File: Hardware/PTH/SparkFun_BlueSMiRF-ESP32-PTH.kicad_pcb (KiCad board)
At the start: 2 copper layers, 38.1 x 15.2 mm, 45 parts, among them J2 Conn_01x06, Q1 Q_NMOS_DGS, Q2 Q_NMOS_DGS, SW1 Switch, U1 ESP32_Pico_Mini, U2 AP2112K-3.3

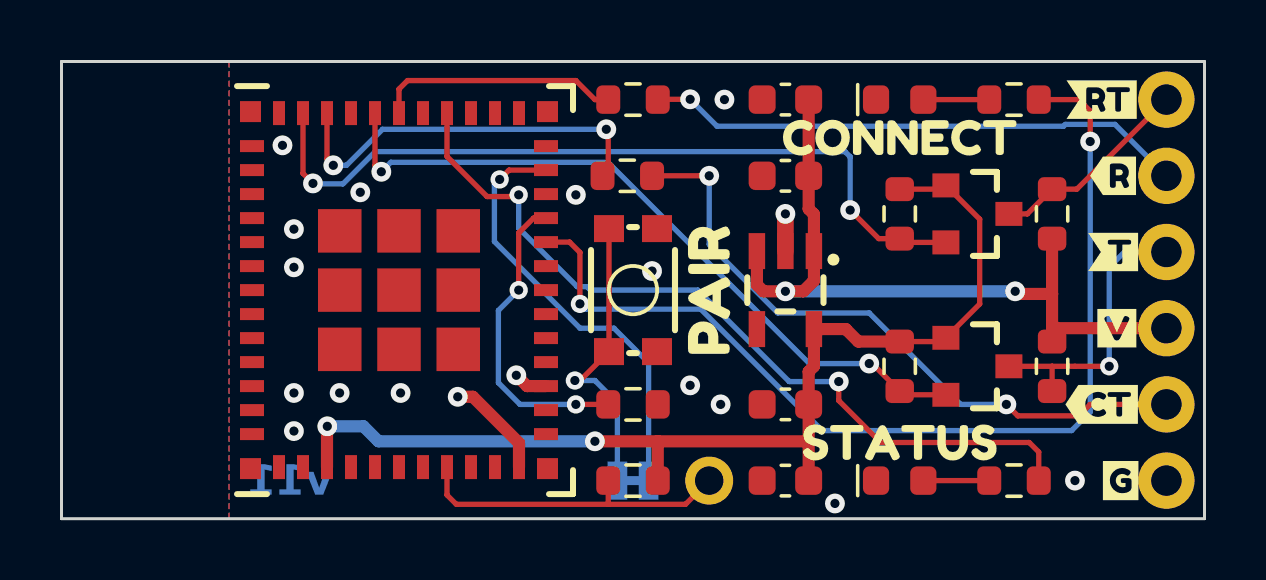
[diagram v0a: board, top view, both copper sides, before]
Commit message: Post design review fixes.
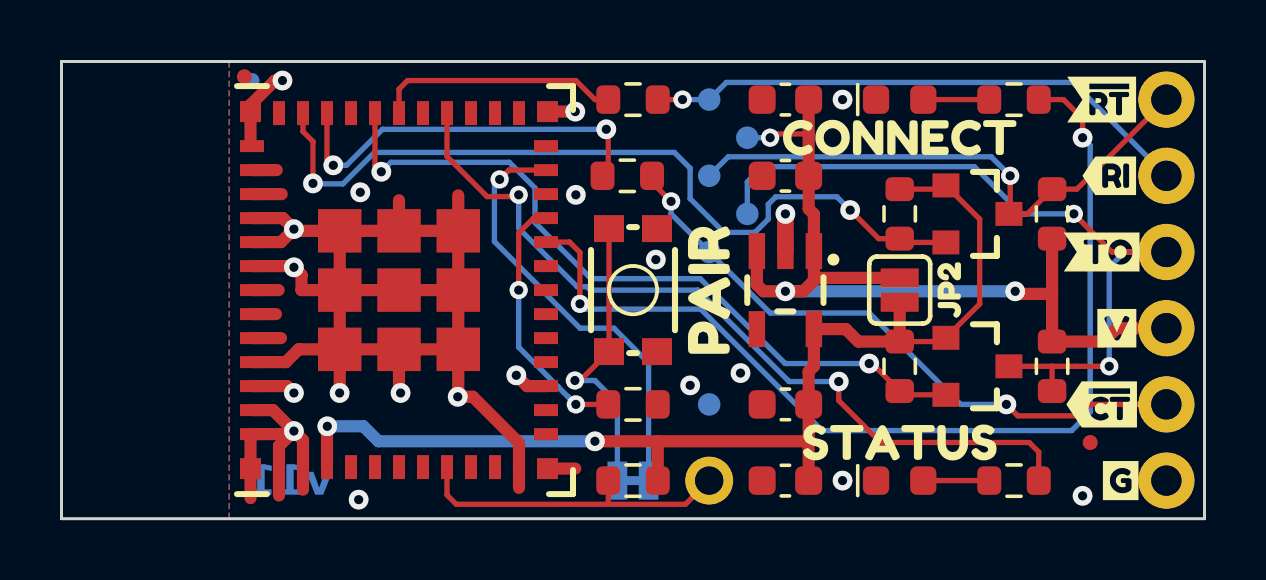
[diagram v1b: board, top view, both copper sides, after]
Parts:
- removed J2: Conn_01x06, SparkFun-Connector:1X06
- removed U3: ~, SparkFun-Aesthetic:ORDERING_INSTRUCTIONS
- removed kibuzzard-65022E62: G***, kibuzzard-65022E62
- removed kibuzzard-65022E77: G***, kibuzzard-65022E77
- removed kibuzzard-65022E81: G***, kibuzzard-65022E81
- removed kibuzzard-65022E99: G***, kibuzzard-65022E99
- removed kibuzzard-65022EA5: G***, kibuzzard-65022EA5
- removed kibuzzard-65022EE4: G***, kibuzzard-65022EE4
- removed kibuzzard-654D17DE: G***, kibuzzard-654D17DE
- removed kibuzzard-654D17E2: G***, kibuzzard-654D17E2
- removed kibuzzard-654D17EE: G***, kibuzzard-654D17EE
- removed kibuzzard-654D17F9: G***, kibuzzard-654D17F9
- added FID1: Fiducial_0.5, SparkFun-Aesthetic:Fiducial_0.5mm_Mask1mm, F.Cu at (135.6, 117.3)
- added FID2: Fiducial_0.5, SparkFun-Aesthetic:Fiducial_0.5mm_Mask1mm, F.Cu at (163.8, 129.5)
- added FID3: Fiducial_0.5, SparkFun-Aesthetic:Fiducial_0.5mm_Mask1mm, B.Cu at (135.9, 117.5)
- added FID4: Fiducial_0.5, SparkFun-Aesthetic:Fiducial_0.5mm_Mask1mm, B.Cu at (160.5, 130.8)
- added J1: Conn_01x06, SparkFun-Connector:1X06, F.Cu at (166.4, 118.1)
- added JP2: ~, SparkFun-Jumper:SMT-JUMPER_2_NO_SILK, F.Cu at (157.5, 124.5)
- added TP2: TestPoint_0.75mm, SparkFun-Connector:TestPoint-0.75mm, B.Cu at (151.1, 118.1)
- added TP3: TestPoint_0.75mm, SparkFun-Connector:TestPoint-0.75mm, B.Cu at (151.1, 123.2)
- added TP4: TestPoint_0.75mm, SparkFun-Connector:TestPoint-0.75mm, B.Cu at (152.4, 121.9)
- added TP5: TestPoint_0.75mm, SparkFun-Connector:TestPoint-0.75mm, B.Cu at (151.1, 120.7)
- added TP6: TestPoint_0.75mm, SparkFun-Connector:TestPoint-0.75mm, B.Cu at (151.1, 128.3)
- added TP7: TestPoint_0.75mm, SparkFun-Connector:TestPoint-0.75mm, B.Cu at (152.4, 119.4)
- added U7: ~, SparkFun-Aesthetic:Ordering_Instructions, F.Cu at (176.6, 81.4)
- added kibuzzard-655A4368: G***, kibuzzard-655A4368, F.Cu at (164.2, 118.1)
- added kibuzzard-655A4384: G***, kibuzzard-655A4384, F.Cu at (164.2, 128.3)
- added kibuzzard-655A4397: G***, kibuzzard-655A4397, B.Cu at (163.3, 128.3)
- added kibuzzard-655A43AA: G***, kibuzzard-655A43AA, B.Cu at (163.3, 118.1)
- added kibuzzard-655A444A: G***, kibuzzard-655A444A, F.Cu at (164.5, 120.7)
- added kibuzzard-655A4470: G***, kibuzzard-655A4470, B.Cu at (163.7, 120.7)
- added kibuzzard-655A4492: G***, kibuzzard-655A4492, B.Cu at (163.3, 123.2)
- added kibuzzard-655A44E1: G***, kibuzzard-655A44E1, F.Cu at (164.2, 123.2)
- added kibuzzard-655A45F8: G***, kibuzzard-655A45F8, B.Cu at (153.3, 130.8)
- added kibuzzard-655A532D: G***, kibuzzard-655A532D, B.Cu at (162.4, 125.7)
- added kibuzzard-655A5C47: G***, kibuzzard-655A5C47, F.Cu at (159.1, 124.5)
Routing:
- net GND: track 6.08 -> 64.7 mm, vias 18 -> 20
- net TX_HV: track 9.59 -> 26.0 mm, vias 1 -> 2
- net RTS_HV: track 6.83 -> 18.7 mm, vias 0 -> 1
- net VCC: track 25.6 -> 30.7 mm, vias 2 -> 3
- net Net-(U1-IOA15): track 10.3 -> 8.70 mm
- net +3.3V: track 36.3 -> 37.6 mm
- net CTS_HV: track 22.1 -> 21.0 mm
- net RTS_LV: track 26.3 -> 27.1 mm
- net TX_LV: track 24.2 -> 24.9 mm
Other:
- board text added: "Copper Weight: 1oz"
- board text added: "Finish: Lead Free HASL"
- board text added: "Material: TG155"
- board text removed: "Finish: HASL Lead Free"

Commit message: Apply design review changes to PTH version.
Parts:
- removed U7: ~, SparkFun-Aesthetic:Ordering_Instructions
- added U3: ~, SparkFun-Aesthetic:ORDERING_INSTRUCTIONS, F.Cu at (0.25, 0.25)
- R10, R3, R4, R7, R8, R9: value 10k -> 1k
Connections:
- net CTS_HV renamed ~{CTS_HV}
- net CTS_LV renamed ~{CTS_LV}
- net RTS_HV renamed ~{RTS_HV}
- net RTS_LV renamed ~{RTS_LV}

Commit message: Change BSS138 resistors to 10k
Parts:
- R1: value 4.7k -> 10k
- R10, R7, R8, R9: value 1k -> 10k
- moved U3 193.5 mm to (176.1, 80.9)
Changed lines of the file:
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@@
   )
   (footprint "SparkFun-Aesthetic:ORDERING_INSTRUCTIONS" (layer "F.Cu")
-    (at 0.25 0.25)
+    (at 176.145 80.895)
     (property "Sheetfile" "SparkFun_BlueSMiRF-ESP32-PTH.kicad_sch")
     (property "Sheetname" "")
@@
     (descr "Resistor SMD 0603 (1608 Metric), square (rectangular) end terminal, IPC_7351 nominal, (Body size source: IPC-SM-782 page 72, https://www.pcb-3d.com/wordpress/wp-content/uploads/ipc-sm-782a_amendment_1_and_2.pdf), generated with kicad-footprint-generator")
     (tags "resistor")
-    (property "PROD_ID" "RES-07856")
+    (property "PROD_ID" "RES-00824")
     (property "Sheetfile" "SparkFun_BlueSMiRF-ESP32-PTH.kicad_sch")
     (property "Sheetname" "")
@@
         (effects (font (size 0.5 0.5) (thickness 0.1) bold))
     )
-    (fp_text value "1k" (at 0 1.43 90) (layer "F.Fab")
+    (fp_text value "10k" (at 0 1.43 90) (layer "F.Fab")
         (effects (font (size 0.5 0.5) (thickness 0.1) bold))
     )
@@
     (descr "Resistor SMD 0603 (1608 Metric), square (rectangular) end terminal, IPC_7351 nominal, (Body size source: IPC-SM-782 page 72, https://www.pcb-3d.com/wordpress/wp-content/uploads/ipc-sm-782a_amendment_1_and_2.pdf), generated with kicad-footprint-generator")
     (tags "resistor")
-    (property "PROD_ID" "RES-07857")
+    (property "PROD_ID" "RES-00824")
     (property "Sheetfile" "SparkFun_BlueSMiRF-ESP32-PTH.kicad_sch")
     (property "Sheetname" "")
@@
         (effects (font (size 0.5 0.5) (thickness 0.1) bold))
     )
-    (fp_text value "4.7k" (at 0 1.43) (layer "F.Fab")
+    (fp_text value "10k" (at 0 1.43) (layer "F.Fab")
         (effects (font (size 0.5 0.5) (thickness 0.1) bold))
     )
@@
     (descr "Resistor SMD 0603 (1608 Metric), square (rectangular) end terminal, IPC_7351 nominal, (Body size source: IPC-SM-782 page 72, https://www.pcb-3d.com/wordpress/wp-content/uploads/ipc-sm-782a_amendment_1_and_2.pdf), generated with kicad-footprint-generator")
     (tags "resistor")
-    (property "PROD_ID" "RES-07856")
+    (property "PROD_ID" "RES-00824")
     (property "Sheetfile" "SparkFun_BlueSMiRF-ESP32-PTH.kicad_sch")
     (property "Sheetname" "")
@@
         (effects (font (size 0.5 0.5) (thickness 0.1) bold))
     )
-    (fp_text value "1k" (at 0 1.43 90) (layer "F.Fab")
+    (fp_text value "10k" (at 0 1.43 90) (layer "F.Fab")
         (effects (font (size 0.5 0.5) (thickness 0.1) bold))
     )
@@
     (descr "Resistor SMD 0603 (1608 Metric), square (rectangular) end terminal, IPC_7351 nominal, (Body size source: IPC-SM-782 page 72, https://www.pcb-3d.com/wordpress/wp-content/uploads/ipc-sm-782a_amendment_1_and_2.pdf), generated with kicad-footprint-generator")
     (tags "resistor")
-    (property "PROD_ID" "RES-07856")
+    (property "PROD_ID" "RES-00824")
     (property "Sheetfile" "SparkFun_BlueSMiRF-ESP32-PTH.kicad_sch")
     (property "Sheetname" "")
@@
         (effects (font (size 0.5 0.5) (thickness 0.1) bold))
     )
-    (fp_text value "1k" (at 0 1.43 90) (layer "F.Fab")
+    (fp_text value "10k" (at 0 1.43 90) (layer "F.Fab")
         (effects (font (size 0.5 0.5) (thickness 0.1) bold))
     )
@@
     (descr "Resistor SMD 0603 (1608 Metric), square (rectangular) end terminal, IPC_7351 nominal, (Body size source: IPC-SM-782 page 72, https://www.pcb-3d.com/wordpress/wp-content/uploads/ipc-sm-782a_amendment_1_and_2.pdf), generated with kicad-footprint-generator")
     (tags "resistor")
-    (property "PROD_ID" "RES-07856")
+    (property "PROD_ID" "RES-00824")
     (property "Sheetfile" "SparkFun_BlueSMiRF-ESP32-PTH.kicad_sch")
     (property "Sheetname" "")
@@
         (effects (font (size 0.5 0.5) (thickness 0.1) bold))
     )
-    (fp_text value "1k" (at 0 1.43 90) (layer "F.Fab")
+    (fp_text value "10k" (at 0 1.43 90) (layer "F.Fab")
         (effects (font (size 0.5 0.5) (thickness 0.1) bold))
     )
@@
     (pts (xy 129.54 116.84) (xy 167.64 116.84))
     (height -2.54)
-    (gr_text "1.50 in" (at 148.59 113.15) (layer "User.1")
+    (gr_text "38.1 mm" (at 148.59 113.15) (layer "User.1")
       (effects (font (size 1 1) (thickness 0.15)))
     )
@@
     (pts (xy 166.37 130.81) (xy 166.37 118.11))
     (height 5.08)
-    (gr_text "0.50 in" (at 170.3 124.46 90) (layer "User.1")
+    (gr_text "12.7 mm" (at 170.3 124.46 90) (layer "User.1")
       (effects (font (size 1 1) (thickness 0.15)))
     )
@@
     (pts (xy 129.54 132.08) (xy 129.54 116.84))
     (height -2.54)
-    (gr_text "0.60 in" (at 125.85 124.46 90) (layer "User.1")
+    (gr_text "15.2 mm" (at 125.85 124.46 90) (layer "User.1")
       (effects (font (size 1 1) (thickness 0.15)))
     )
